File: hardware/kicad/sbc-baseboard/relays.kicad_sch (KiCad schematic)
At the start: 30 parts, among them J11 Relay COM/NO/NC, J12 Relay COM/NO/NC, J18 PSU in (isolated), J19 PSU out (isolated), K801 G6K-2F-Y DC5, K802 G6K-2F-Y DC5, K803 JW1FSN-DC5V, Q801 2N7002, Q802 2N7002, Q803 AO3400A, U801 LTV-817

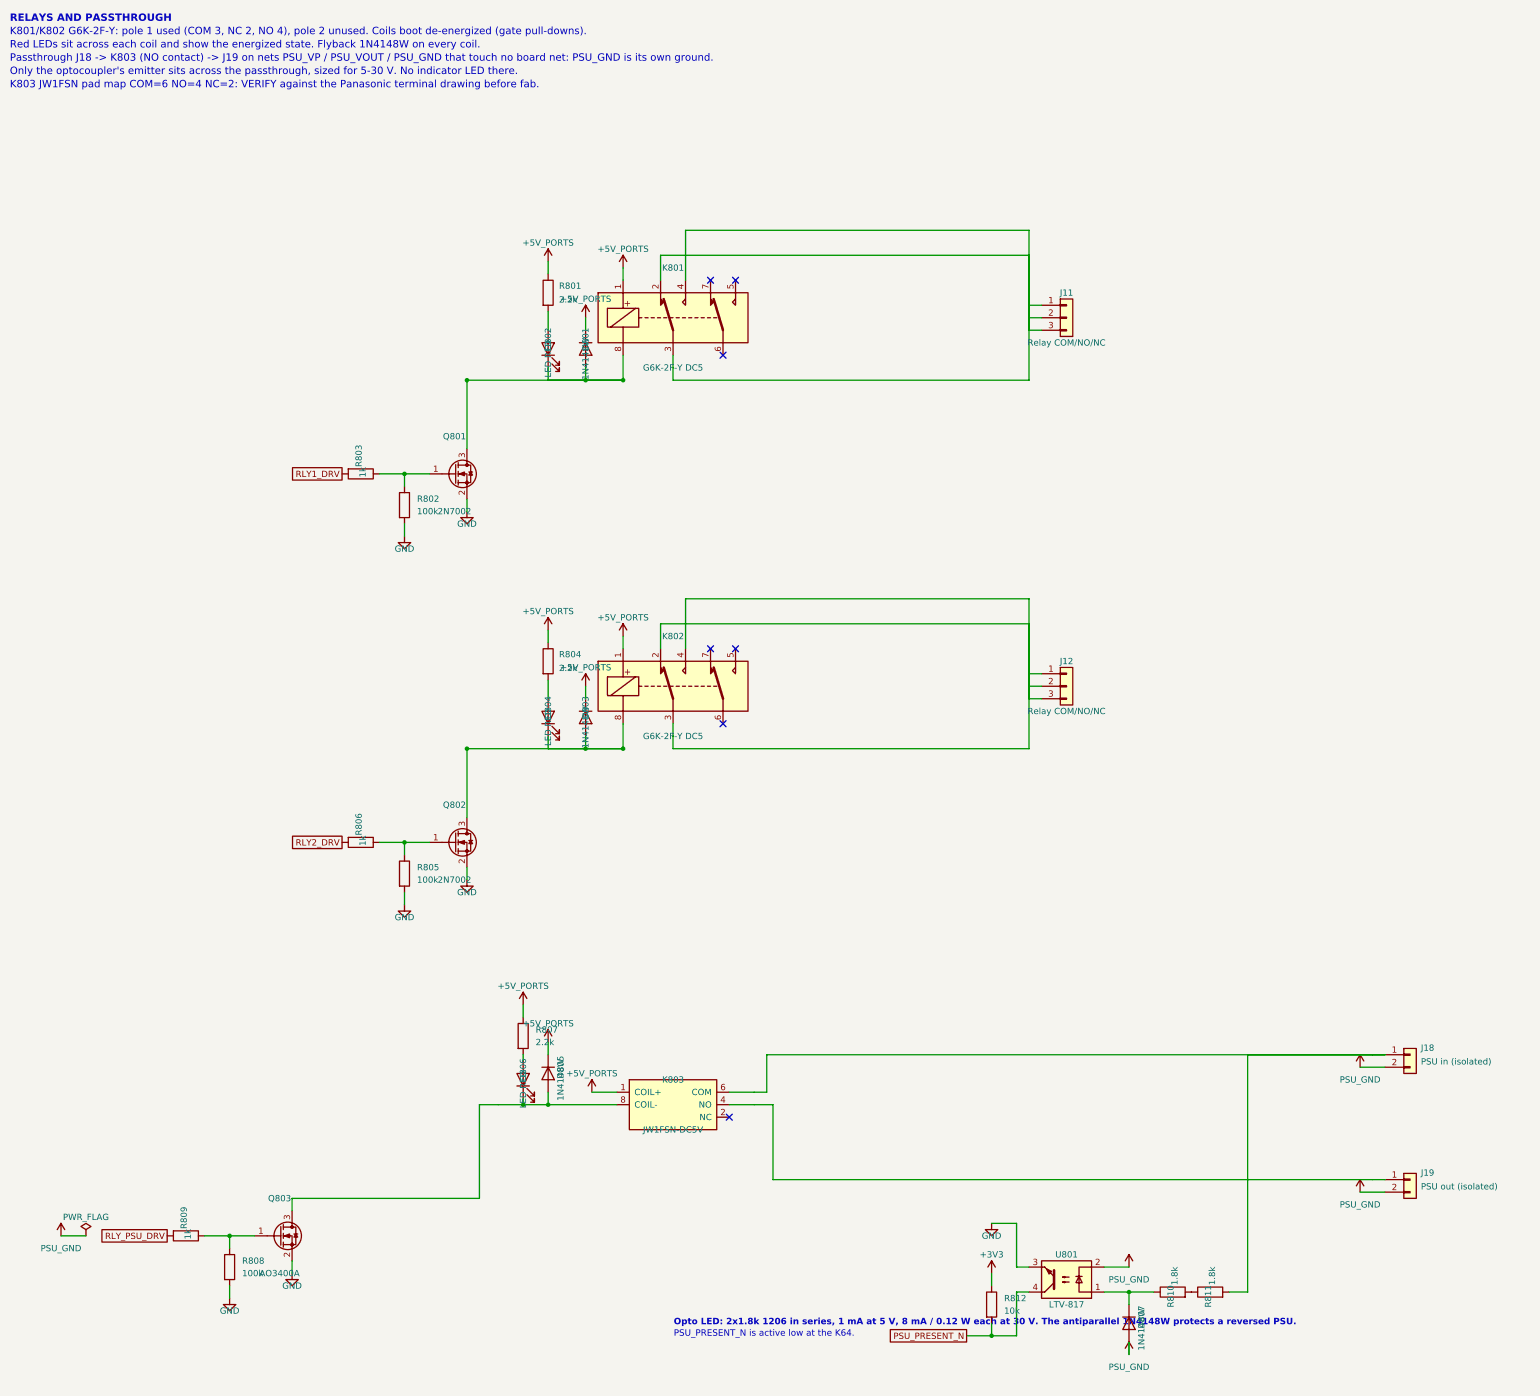
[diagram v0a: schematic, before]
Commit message: Symbol direction, field text and decoupling ladders across every sheet
Every GND symbol now hangs down and every rail stands up: decoupling
hangs from the supply bus into a GND rail with one GND symbol at the end
(ladders), rails on crowded supply pins are jogged sideways, the SWD
header is mirrored instead of rotated. Field text on in-line parts reads
horizontally (KiCad adds the symbol rotation to the field angle) and is
placed by lane direction; hanging parts carry their text on the side away
from the pin; IC reference and value sit where the library put them.
Power sheet: bus buffer moved under the STUSB4500's I2C lanes with direct
routes, programmer by label, buck drawn as a box with its input and
output capacitors as ladders. New gen/check_layout.py reports text and
wire overlaps and wrong-way power symbols; PDF export draws hop-overs.

ERC 0, no merged rails, netlist equivalent; text-overlap residue listed
in the layout checker output remains on the hub, relays and DAPLink.

Co-Authored-By: Claude Fable 5.1 <noreply@anthropic.com>
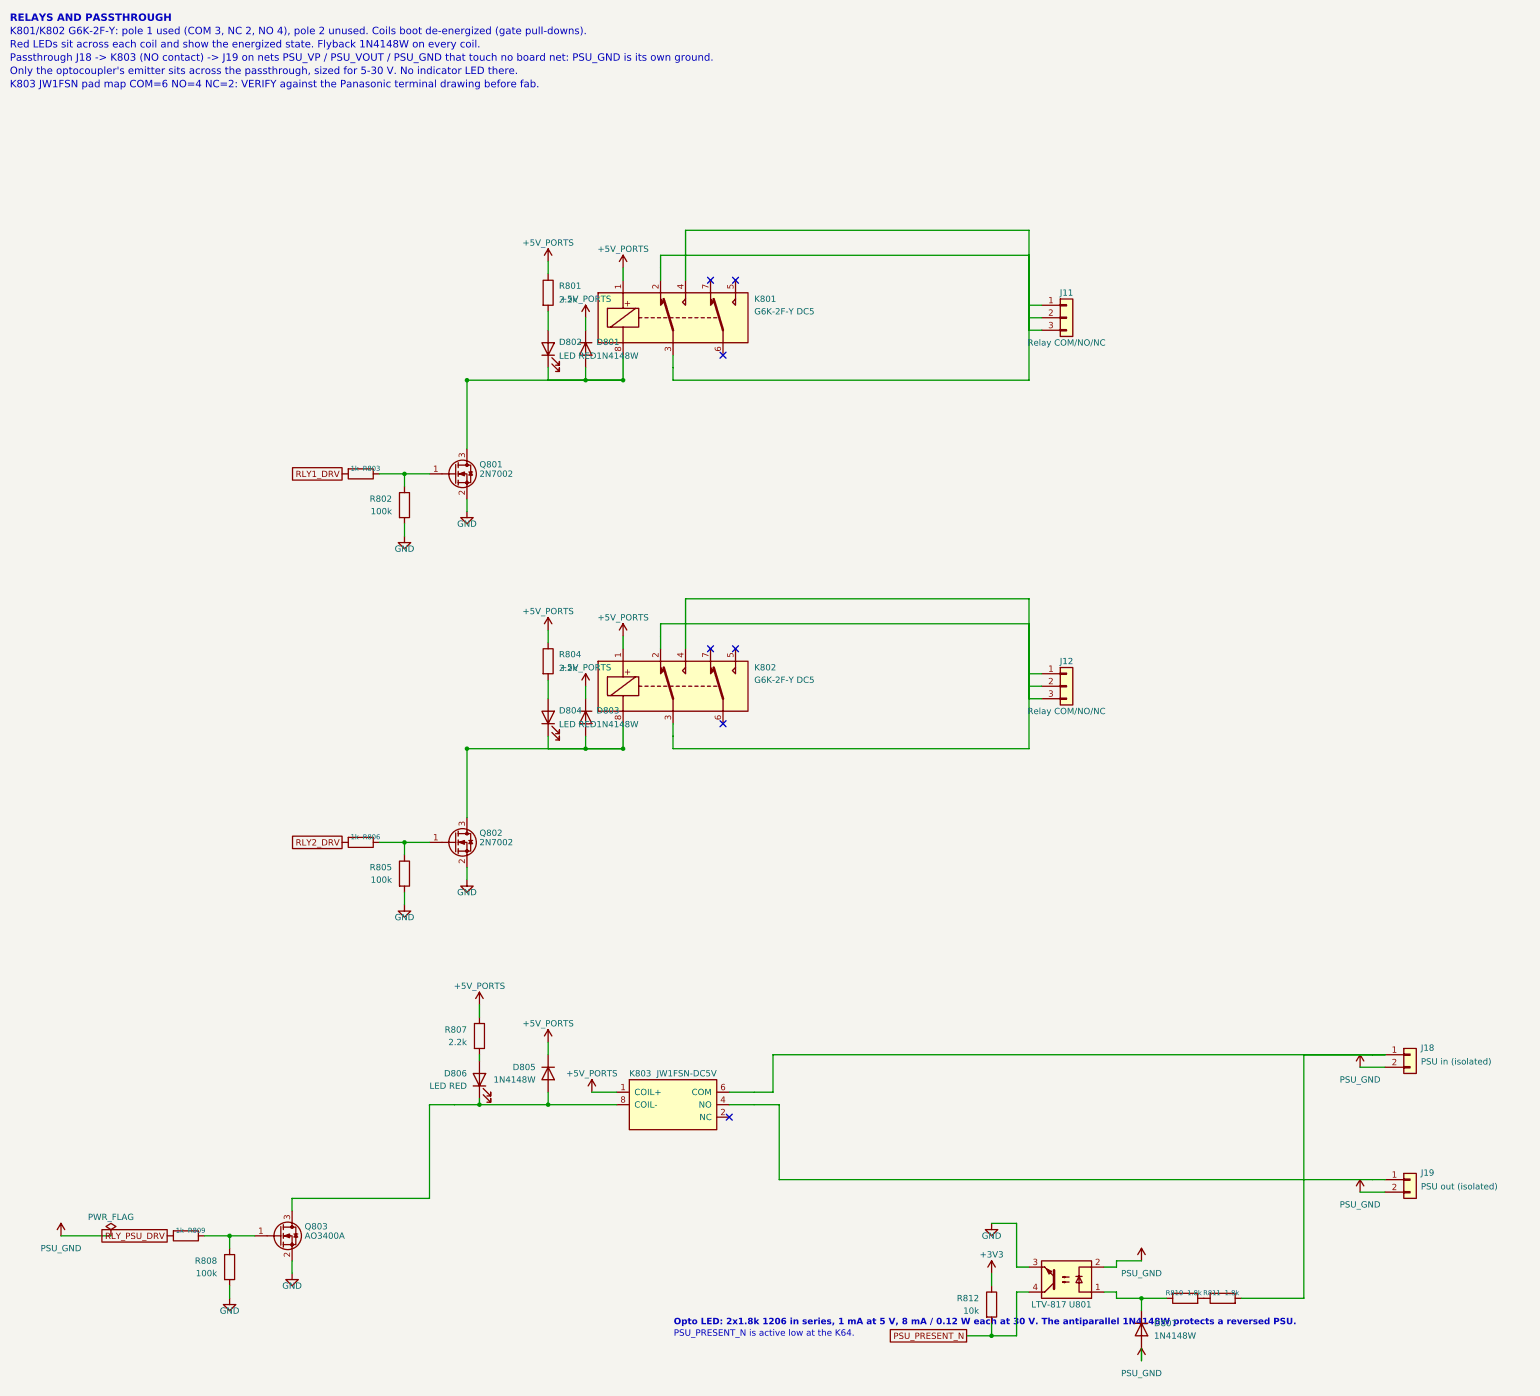
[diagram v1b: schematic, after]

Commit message: Placement pass: every sheet clean on all four layout gates
Hanging parts now sit with their near pin between rows, so a pull-up on
the next lane crosses only its lead; parts slide past a neighbour's parts
and text, not its plain wire, and never let a wire run through a body or
a rail symbol. Chains on top/bottom pins run sideways first. Route
channels are numbered per route. Power symbols that would land on a
neighbouring wire get a jog or a hook. The VBUS sense divider moved to
the K64's ADC pin so J3's VBUS lane is a short stretch the ESD array taps;
the J1 tap sits before its divider. Relay coil clusters are drawn by the
engine. Port switches moved so OUT stays on the VBUS row.

ERC 0, no endpoint contacts, no merged rails, no wires through bodies,
no inverted power symbols, on all eight sheets; netlist equivalent to the
first pass (331 parts, 354 nets); USB D+/D-, VBUS and I2C paths verified
pin by pin.

Co-Authored-By: Claude Fable 5.1 <noreply@anthropic.com>
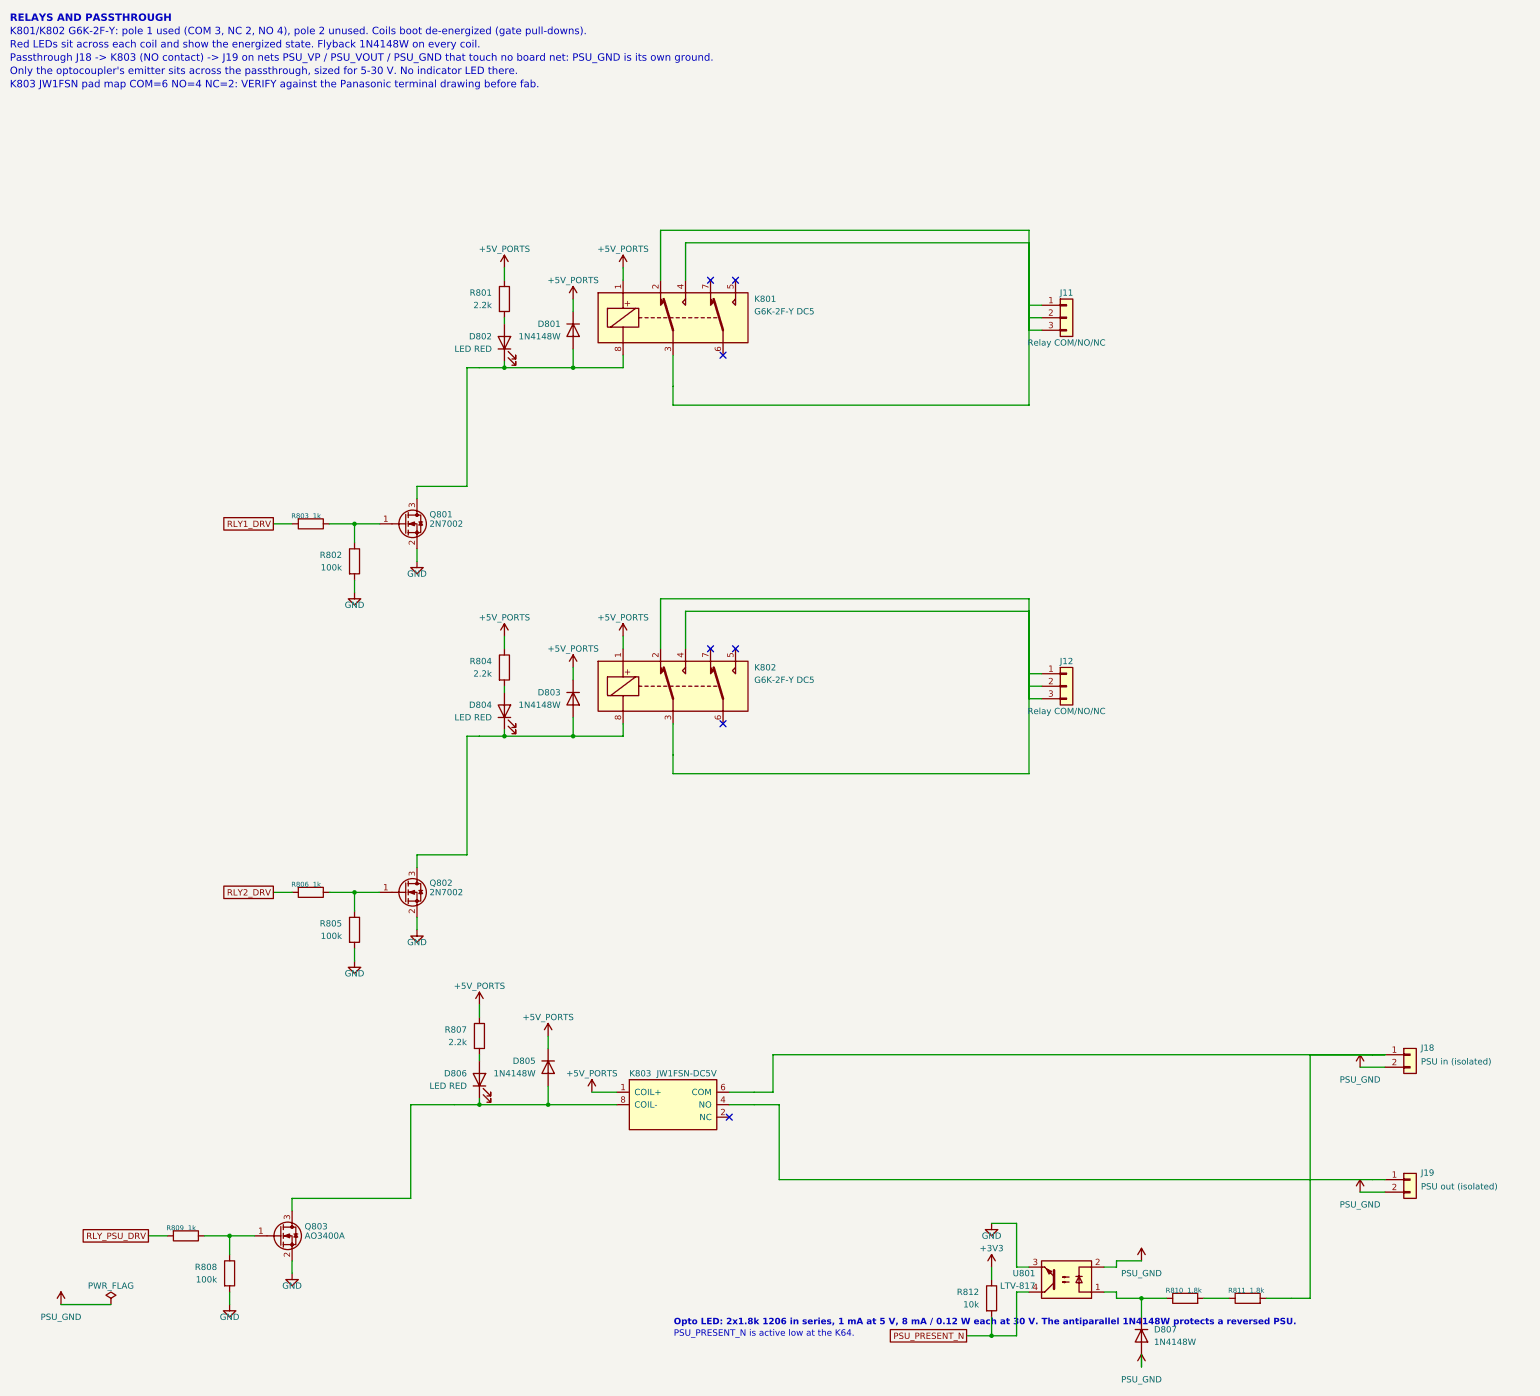
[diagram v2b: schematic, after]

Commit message: Symbol name clearance, divider at the reading pin, inlet TVS orientation
Symbols: a top or bottom pin's name runs vertically into the body, so box
symbols now grow outward by whole rows wherever such a name would reach a
side pin's name (USB2517 three rows on top, K64 two rows top and bottom,
PCA9517A three rows on top); the side-pin rows stay where they were so the
sheet layouts are unaffected. U402's VDD names no longer print over USBUP_DP.

Frame pass: nothing on the sheet frame or the title block, enforced by the
layout gate (usable area 15..405 x 15..282 mm, title block from 300/253).

Flow pass: pull-ups hang up to their rail, pull-downs hang down (R408/R409
and the other strap and sense resistors). The J1 VBUS_DET divider sits at
U402 pin 44, the pin that reads it; J1's VBUS lane is a plain stretch that
U401 taps; J1 and U401 lifted clear of the hub's +3V3 bus. The hub's left
strap lanes turn in columns starting at x = 118.11 so they clear the bottom
decoupling ladders (fan() grew a turn_at argument for this).

Inlet TVS D102 hangs from J2's VBUS lane as a D_Zener with its cathode on
VBUS_IN. At 8579cd2 it was drawn with the bidirectional D_TVS symbol and
pad 1 (the SMA cathode) on GND, which would have forward-biased it.

Bucks: the FB pulls start past the catch diode's text; the two notes are
rewrapped and sit between U101 and the compensation parts.

Gates on every sheet: ERC 0, endpoint contacts 0, rail merges 0, frame 0,
no text on bodies or wires. Connectivity identical to 8579cd2 (symmetric
passives order-free) except the TVS orientation.

Co-Authored-By: Claude Fable 5.1 <noreply@anthropic.com>
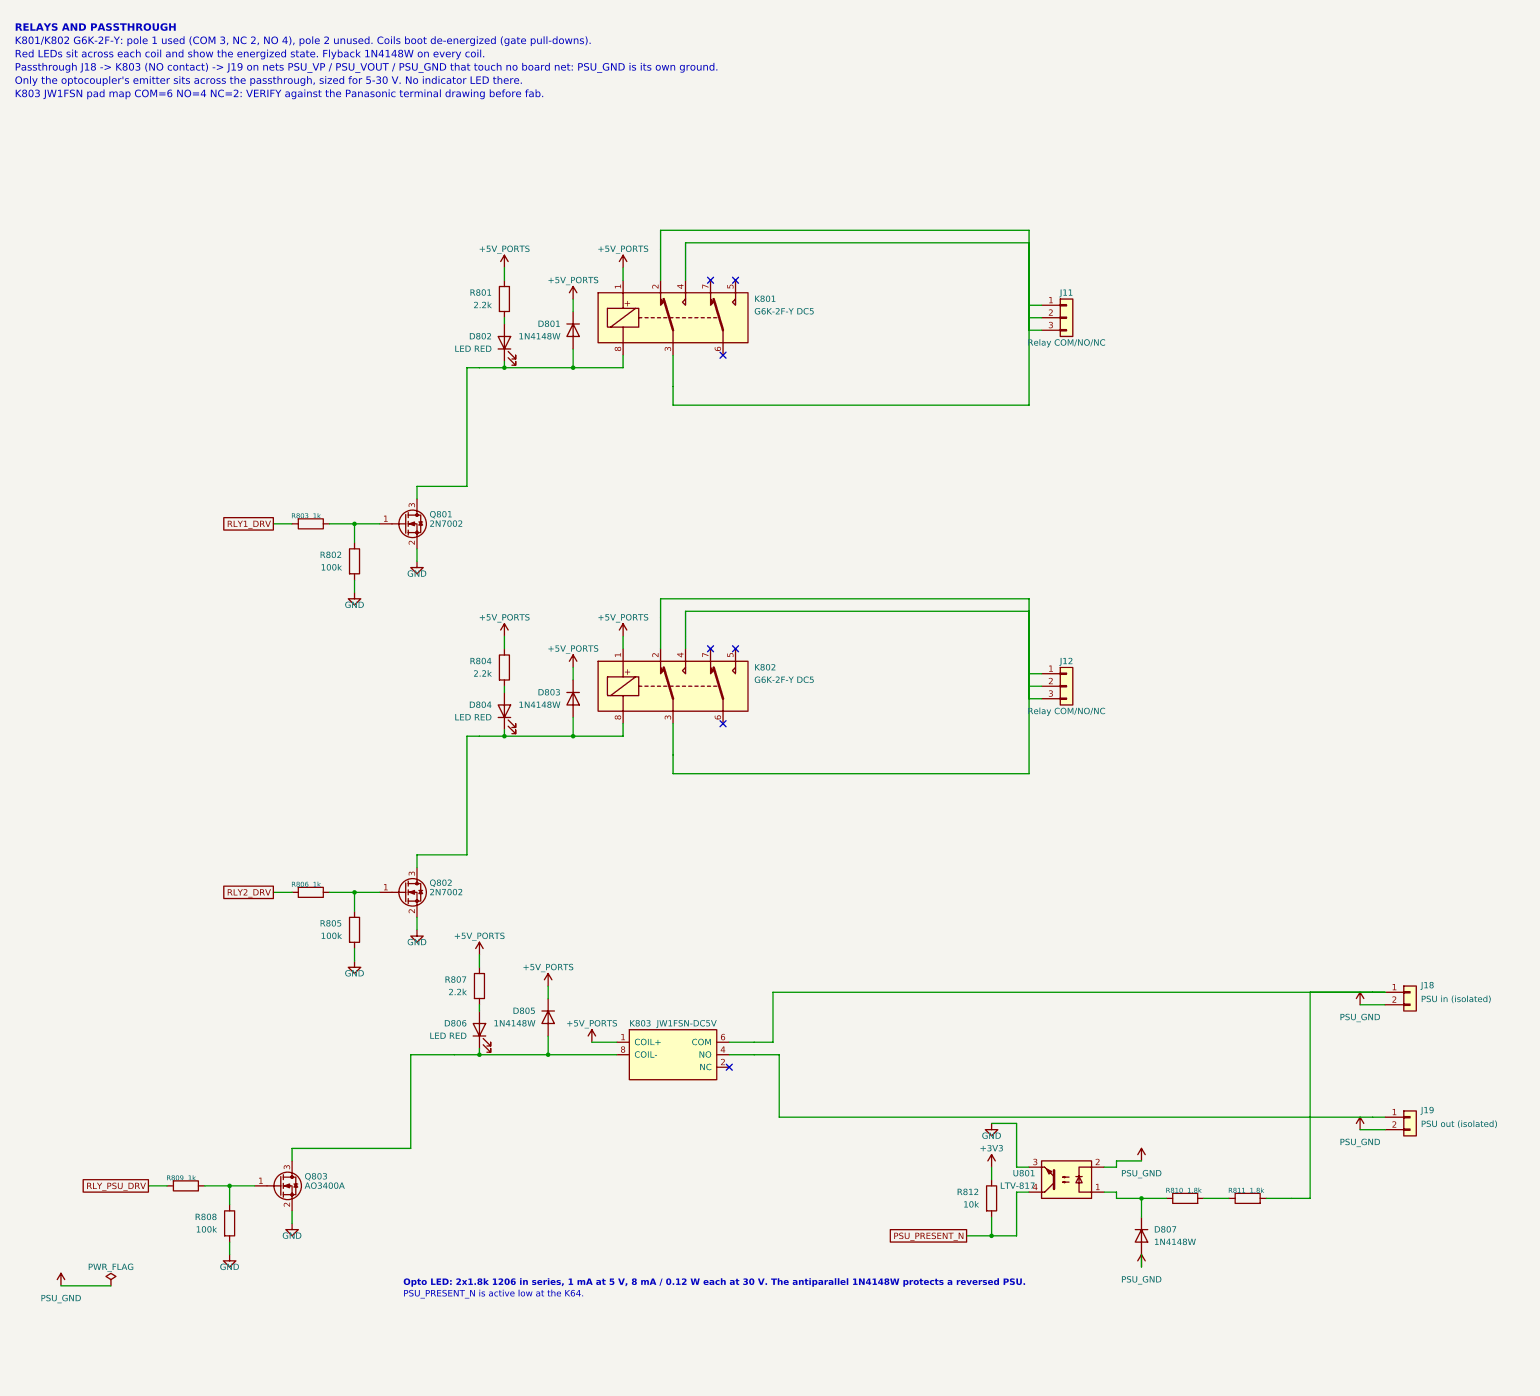
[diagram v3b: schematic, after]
